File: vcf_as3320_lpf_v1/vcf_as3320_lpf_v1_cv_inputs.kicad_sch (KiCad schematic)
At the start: 32 parts, among them U1 LM358, U5 LM358

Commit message: Draft layout done no routing
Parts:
- removed J_FREQ1, J_FREQ2: FREQ, My Stuff:Jack_3.5mm_MJ-355W_and_PJ398SM_Vertical, symbol Connector:AudioJack2_SwitchT
- added J_FREQ1: FREQ, My Stuff:Jack_3.5mm_MJ-355W_Vertical, symbol Connector:AudioJack3
- added J_RES1: RES, My Stuff:Jack_3.5mm_MJ-355W_Vertical, symbol Connector:AudioJack3
- D1, D4: footprint Diode_THT:D_A-405_P7.62mm_Horizontal -> Diode_THT:D_A-405_P2.54mm_Vertical_KathodeUp
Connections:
- net GND: now also J_FREQ1.S, J_RES1.S
- net at R_FREQ1.1: now also R1.2; no longer R2.1
- net at R4.1, R_FREQ1.2: now also J_FREQ1.T
- net at R_FREQ1.3: now also R2.1; no longer R1.2
- net at R24.1, R_RES1.2: now also J_RES1.T
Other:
- note added: "Flipped since higher voltages lower filter freq."
- moved on the sheet: R_FREQ1
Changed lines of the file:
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@@
   (junction (at 199.39 111.76) (diameter 0) (color 0 0 0 0)
   )
-  (no_connect (at 106.68 119.38))
-  (no_connect (at 104.14 81.534))
+  (no_connect (at 106.68 114.3))
+  (no_connect (at 104.14 76.454))
   (wire (pts (xy 72.39 86.36) (xy 83.82 86.36))
     (stroke (width 0) (type default) (color 0 0 0 0))
@@
   )
   (text "https://tinyurl.com/255uf7kc" (at 158.496 64.77 0)
+    (effects (font (size 1.27 1.27)) (justify left bottom))
+  )
+  (text "Flipped since higher voltages lower filter freq." (at 104.902 55.118 0)
     (effects (font (size 1.27 1.27)) (justify left bottom))
   )
@@
     (pin "2")
   )
-  (symbol (lib_id "power:GND") (at 104.14 76.454 90) (unit 1)
-    (in_bom yes) (on_board yes)
-    (property "Reference" "#PWR025" (id 0) (at 110.49 76.454 0)
-      (effects (font (size 1.27 1.27)) hide)
-    )
-    (property "Value" "GND" (id 1) (at 108.5342 76.327 0))
-    (property "Footprint" "" (id 2) (at 104.14 76.454 0)
-      (effects (font (size 1.27 1.27)) hide)
-    )
-    (property "Datasheet" "" (id 3) (at 104.14 76.454 0)
+  (symbol (lib_id "power:GND") (at 104.14 73.914 90) (unit 1)
+    (in_bom yes) (on_board yes)
+    (property "Reference" "#PWR025" (id 0) (at 110.49 73.914 0)
+      (effects (font (size 1.27 1.27)) hide)
+    )
+    (property "Value" "GND" (id 1) (at 108.5342 73.787 0))
+    (property "Footprint" "" (id 2) (at 104.14 73.914 0)
+      (effects (font (size 1.27 1.27)) hide)
+    )
+    (property "Datasheet" "" (id 3) (at 104.14 73.914 0)
       (effects (font (size 1.27 1.27)) hide)
     )
@@
     (pin "2")
   )
-  (symbol (lib_id "Device:R_Potentiometer_MountingPin") (at 119.38 68.834 270) (unit 1)
-    (in_bom yes) (on_board yes)
-    (property "Reference" "R_FREQ1" (id 0) (at 119.38 63.5762 90))
-    (property "Value" "100k" (id 1) (at 119.38 65.8876 90))
+  (symbol (lib_id "Device:R_Potentiometer_MountingPin") (at 119.38 68.834 90) (mirror x) (unit 1)
+    (in_bom yes) (on_board yes)
+    (property "Reference" "R_FREQ1" (id 0) (at 120.142 59.182 90))
+    (property "Value" "100k" (id 1) (at 119.634 57.15 90))
     (property "Footprint" "My Stuff:Potentiometer_Alpha_RD901F-40-00D_Single_Vertical_w_3d" (id 2) (at 119.38 68.834 0)
       (effects (font (size 1.27 1.27)) hide)
@@
     (pin "2")
   )
-  (symbol (lib_id "power:GND") (at 119.38 63.754 180) (unit 1)
-    (in_bom yes) (on_board yes)
-    (property "Reference" "#PWR019" (id 0) (at 119.38 57.404 0)
-      (effects (font (size 1.27 1.27)) hide)
-    )
-    (property "Value" "GND" (id 1) (at 120.65 61.214 0)
-      (effects (font (size 1.27 1.27)) (justify right))
-    )
-    (property "Footprint" "" (id 2) (at 119.38 63.754 0)
-      (effects (font (size 1.27 1.27)) hide)
-    )
-    (property "Datasheet" "" (id 3) (at 119.38 63.754 0)
-      (effects (font (size 1.27 1.27)) hide)
-    )
-    (pin "1")
-  )
-  (symbol (lib_id "Connector:AudioJack2_SwitchT") (at 99.06 78.994 0) (unit 1)
-    (in_bom yes) (on_board yes) (fields_autoplaced)
-    (property "Reference" "J_FREQ1" (id 0) (at 98.425 71.2175 0))
-    (property "Value" "FREQ" (id 1) (at 98.425 73.9926 0))
-    (property "Footprint" "My Stuff:Jack_3.5mm_MJ-355W_and_PJ398SM_Vertical" (id 2) (at 99.06 78.994 0)
-      (effects (font (size 1.27 1.27)) hide)
-    )
-    (property "Datasheet" "~" (id 3) (at 99.06 78.994 0)
-      (effects (font (size 1.27 1.27)) hide)
-    )
+  (symbol (lib_id "Connector:AudioJack3") (at 101.6 114.3 0) (unit 1)
+    (in_bom yes) (on_board yes)
+    (property "Reference" "J_RES1" (id 0) (at 102.616 107.442 0)
+      (effects (font (size 1.27 1.27)) (justify right))
+    )
+    (property "Value" "RES" (id 1) (at 101.092 109.474 0)
+      (effects (font (size 1.27 1.27)) (justify right))
+    )
+    (property "Footprint" "My Stuff:Jack_3.5mm_MJ-355W_Vertical" (id 2) (at 101.6 114.3 0)
+      (effects (font (size 1.27 1.27)) hide)
+    )
+    (property "Datasheet" "~" (id 3) (at 101.6 114.3 0)
+      (effects (font (size 1.27 1.27)) hide)
+    )
+    (pin "R")
     (pin "S")
     (pin "T")
-    (pin "TN")
+  )
+  (symbol (lib_id "power:GND") (at 119.38 63.754 180) (unit 1)
+    (in_bom yes) (on_board yes)
+    (property "Reference" "#PWR019" (id 0) (at 119.38 57.404 0)
+      (effects (font (size 1.27 1.27)) hide)
+    )
+    (property "Value" "GND" (id 1) (at 120.65 61.214 0)
+      (effects (font (size 1.27 1.27)) (justify right))
+    )
+    (property "Footprint" "" (id 2) (at 119.38 63.754 0)
+      (effects (font (size 1.27 1.27)) hide)
+    )
+    (property "Datasheet" "" (id 3) (at 119.38 63.754 0)
+      (effects (font (size 1.27 1.27)) hide)
+    )
+    (pin "1")
   )
   (symbol (lib_id "Device:R") (at 130.81 106.68 90) (unit 1)
@@
     (property "Reference" "D4" (id 0) (at 146.05 111.3282 0))
     (property "Value" "D" (id 1) (at 146.05 113.6396 0))
-    (property "Footprint" "Diode_THT:D_A-405_P7.62mm_Horizontal" (id 2) (at 146.05 116.84 0)
+    (property "Footprint" "Diode_THT:D_A-405_P2.54mm_Vertical_KathodeUp" (id 2) (at 146.05 116.84 0)
       (effects (font (size 1.27 1.27)) hide)
     )
@@
     (property "Reference" "D1" (id 0) (at 143.51 73.4822 0))
     (property "Value" "D" (id 1) (at 143.51 75.7936 0))
-    (property "Footprint" "Diode_THT:D_A-405_P7.62mm_Horizontal" (id 2) (at 143.51 78.994 0)
+    (property "Footprint" "Diode_THT:D_A-405_P2.54mm_Vertical_KathodeUp" (id 2) (at 143.51 78.994 0)
       (effects (font (size 1.27 1.27)) hide)
     )
@@
     (pin "1")
   )
+  (symbol (lib_id "Connector:AudioJack3") (at 99.06 76.454 0) (unit 1)
+    (in_bom yes) (on_board yes)
+    (property "Reference" "J_FREQ1" (id 0) (at 101.346 69.088 0)
+      (effects (font (size 1.27 1.27)) (justify right))
+    )
+    (property "Value" "FREQ" (id 1) (at 99.822 71.12 0)
+      (effects (font (size 1.27 1.27)) (justify right))
+    )
+    (property "Footprint" "My Stuff:Jack_3.5mm_MJ-355W_Vertical" (id 2) (at 99.06 76.454 0)
+      (effects (font (size 1.27 1.27)) hide)
+    )
+    (property "Datasheet" "~" (id 3) (at 99.06 76.454 0)
+      (effects (font (size 1.27 1.27)) hide)
+    )
+    (pin "R")
+    (pin "S")
+    (pin "T")
+  )
   (symbol (lib_id "Device:R") (at 207.01 82.804 270) (unit 1)
     (in_bom yes) (on_board yes)
@@
     (pin "2")
   )
-  (symbol (lib_id "power:GND") (at 106.68 114.3 90) (unit 1)
-    (in_bom yes) (on_board yes)
-    (property "Reference" "#PWR035" (id 0) (at 113.03 114.3 0)
-      (effects (font (size 1.27 1.27)) hide)
-    )
-    (property "Value" "GND" (id 1) (at 111.0742 114.173 0))
-    (property "Footprint" "" (id 2) (at 106.68 114.3 0)
-      (effects (font (size 1.27 1.27)) hide)
-    )
-    (property "Datasheet" "" (id 3) (at 106.68 114.3 0)
+  (symbol (lib_id "power:GND") (at 106.68 111.76 90) (unit 1)
+    (in_bom yes) (on_board yes)
+    (property "Reference" "#PWR035" (id 0) (at 113.03 111.76 0)
+      (effects (font (size 1.27 1.27)) hide)
+    )
+    (property "Value" "GND" (id 1) (at 111.0742 111.633 0))
+    (property "Footprint" "" (id 2) (at 106.68 111.76 0)
+      (effects (font (size 1.27 1.27)) hide)
+    )
+    (property "Datasheet" "" (id 3) (at 106.68 111.76 0)
       (effects (font (size 1.27 1.27)) hide)
     )
@@
     (pin "2")
   )
-  (symbol (lib_id "Connector:AudioJack2_SwitchT") (at 101.6 116.84 0) (unit 1)
-    (in_bom yes) (on_board yes) (fields_autoplaced)
-    (property "Reference" "J_FREQ2" (id 0) (at 100.965 109.0635 0))
-    (property "Value" "FREQ" (id 1) (at 100.965 111.8386 0))
-    (property "Footprint" "My Stuff:Jack_3.5mm_MJ-355W_and_PJ398SM_Vertical" (id 2) (at 101.6 116.84 0)
-      (effects (font (size 1.27 1.27)) hide)
-    )
-    (property "Datasheet" "~" (id 3) (at 101.6 116.84 0)
-      (effects (font (size 1.27 1.27)) hide)
-    )
-    (pin "S")
-    (pin "T")
-    (pin "TN")
-  )
 )

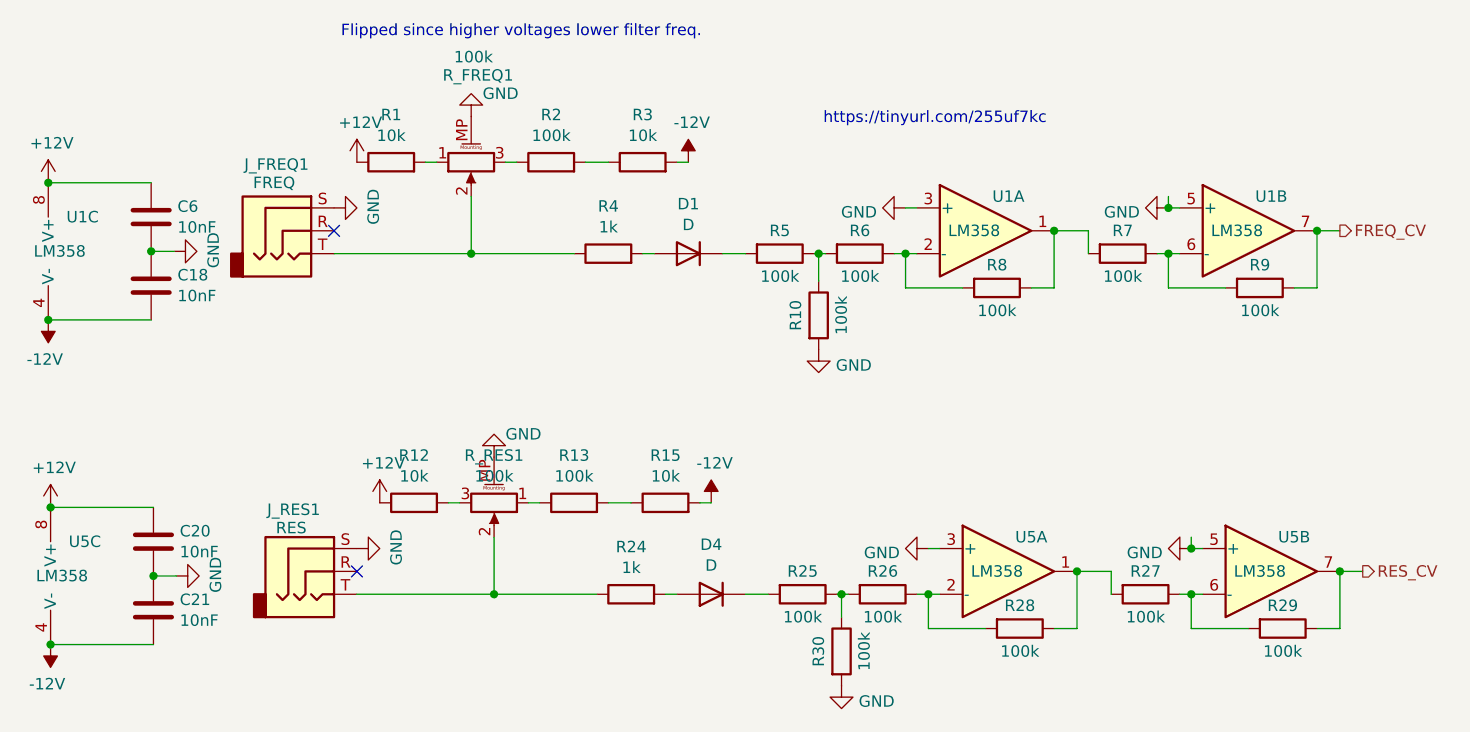
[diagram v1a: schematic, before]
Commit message: Geographic rename, silkscreen cleanup
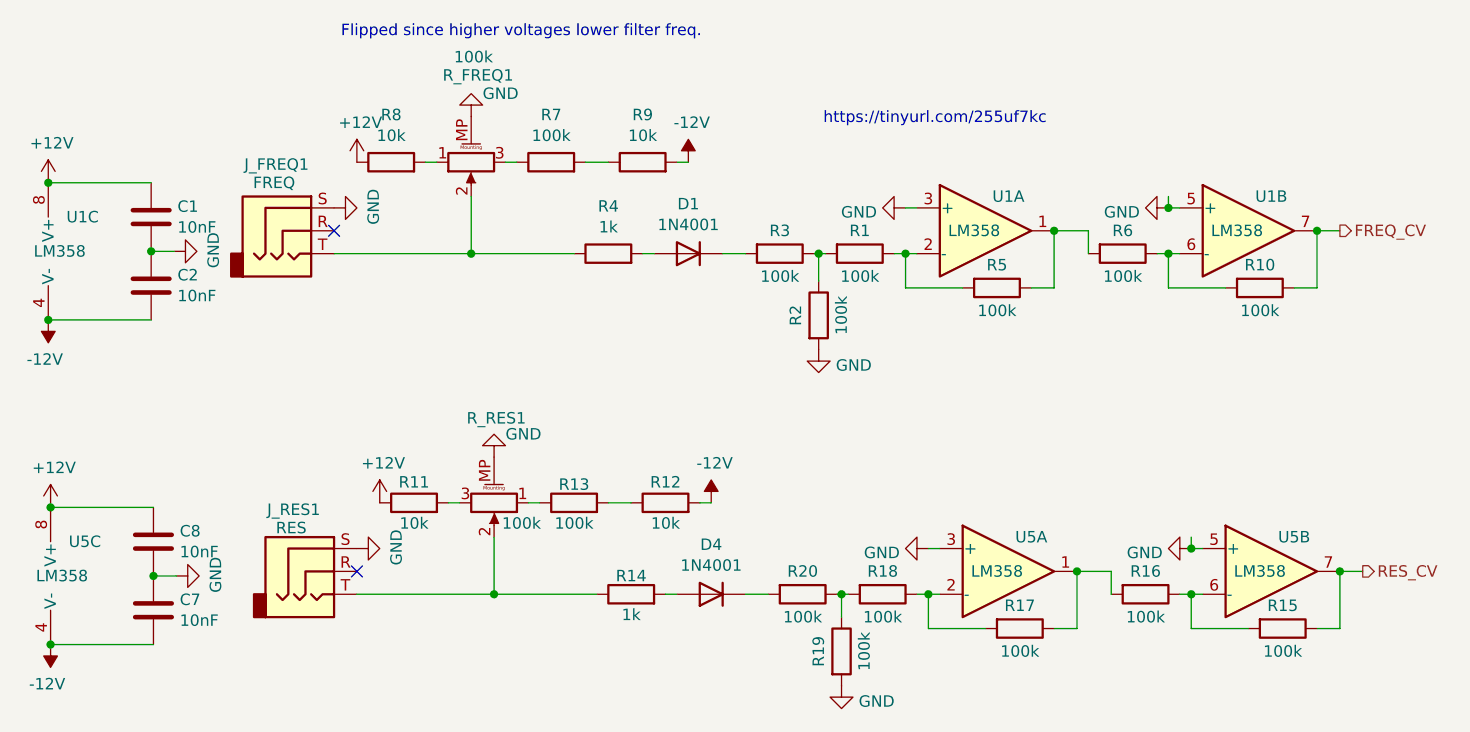
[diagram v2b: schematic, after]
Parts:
- D1, D4: value D -> 1N4001
- renumbered C6 to C1, C18 to C2, C21 to C7, C20 to C8, R6 to R1, R9 to R10, R12 to R11, R15 to R12, R24 to R14, R29 to R15, R27 to R16, R28 to R17, R26 to R18, R30 to R19, R10 to R2, R25 to R20, R5 to R3, R8 to R5, R7 to R6, R2 to R7, R1 to R8, R3 to R9
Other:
- company: (none) -> RobotDialogs
- title: (none) -> VCF AS3320
